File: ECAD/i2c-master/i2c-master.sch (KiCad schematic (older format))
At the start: 19 parts, among them J1 Conn_01x12_Female, J10 Conn_01x04, J11 Barrel_Jack, J12 Conn_02x10_Odd_Even, J2 Conn_01x04, J3 Conn_01x04, J4 Conn_01x04, J5 Conn_01x04, J6 Conn_01x12_Female, J7 Conn_01x04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

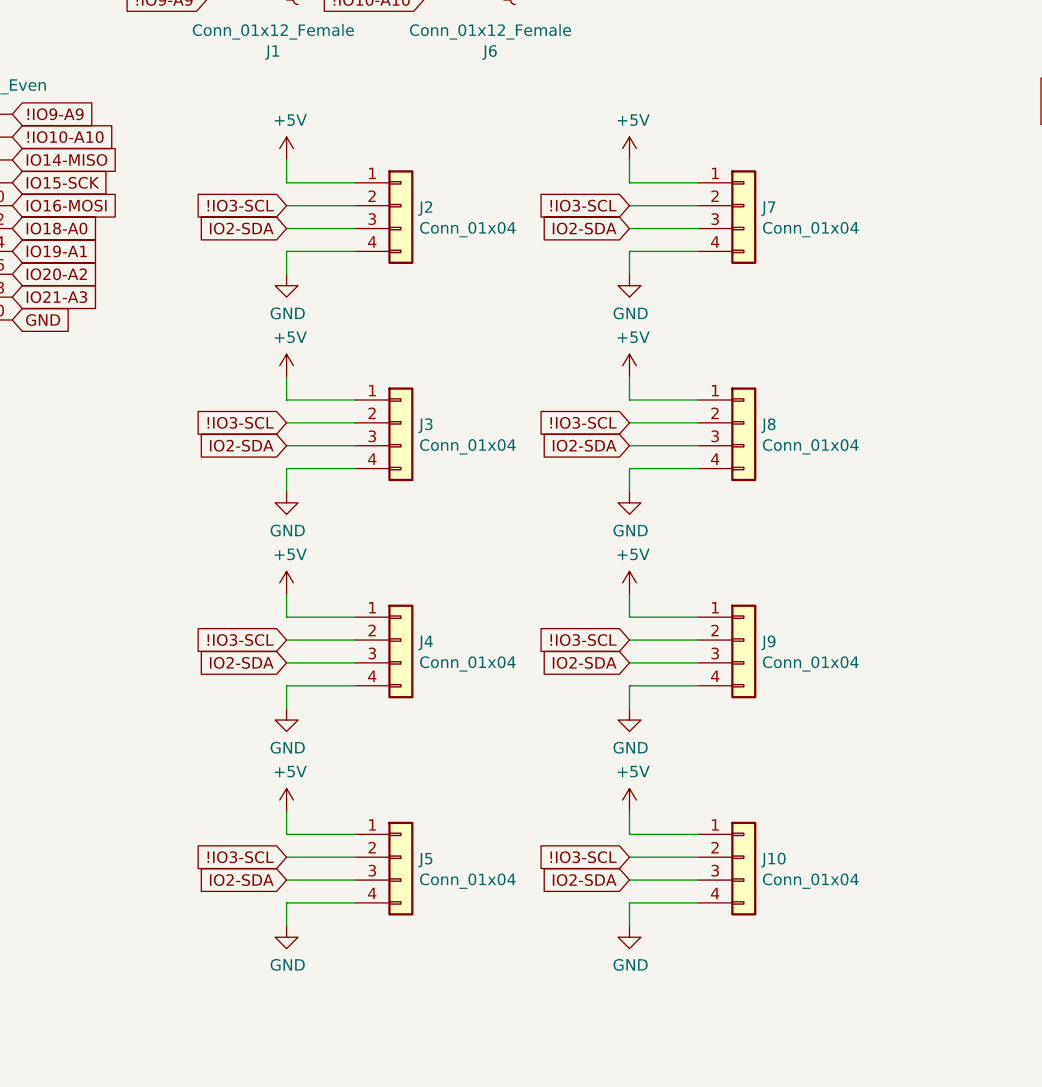
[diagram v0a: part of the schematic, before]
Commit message: Change from 1x04 2.54mm headers to 1x05 micro JST
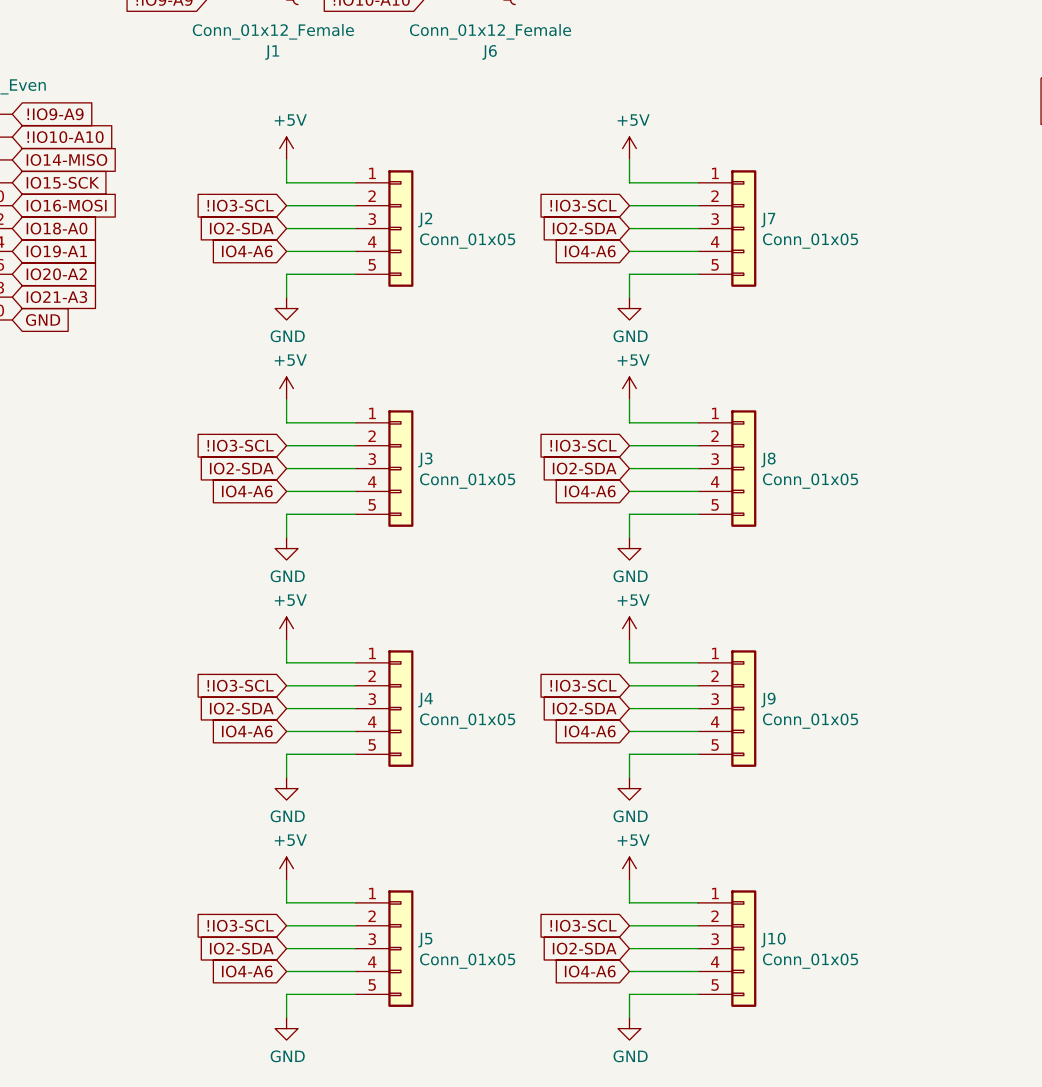
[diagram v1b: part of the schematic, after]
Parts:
- removed J10, J2, J3, J4, J5, J7, J8, J9: Conn_01x04, Connector_PinHeader_2.54mm:PinHeader_1x04_P2.54mm_Vertical, symbol Connector_Generic:Conn_01x04
- added J10, J2, J3, J4, J5, J7, J8, J9: Conn_01x05, Connector_JST:JST_GH_BM05B-GHS-TBT_1x05-1MP_P1.25mm_Vertical, symbol Connector_Generic:Conn_01x05
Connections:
- net !IO3-SCL: now also J10.2 (Pin_2), J2.2 (Pin_2), J3.2 (Pin_2), J4.2 (Pin_2), J5.2 (Pin_2), J7.2 (Pin_2), J8.2 (Pin_2), J9.2 (Pin_2)
- net +5V: now also J10.1 (Pin_1), J2.1 (Pin_1), J3.1 (Pin_1), J4.1 (Pin_1), J5.1 (Pin_1), J7.1 (Pin_1), J8.1 (Pin_1), J9.1 (Pin_1)
- net GND: now also J10.5 (Pin_5), J2.5 (Pin_5), J3.5 (Pin_5), J4.5 (Pin_5), J5.5 (Pin_5), J7.5 (Pin_5), J8.5 (Pin_5), J9.5 (Pin_5)
- net IO2-SDA: now also J10.3 (Pin_3), J2.3 (Pin_3), J3.3 (Pin_3), J4.3 (Pin_3), J5.3 (Pin_3), J7.3 (Pin_3), J8.3 (Pin_3), J9.3 (Pin_3)
- net IO4-A6: now also J10.4 (Pin_4), J2.4 (Pin_4), J3.4 (Pin_4), J4.4 (Pin_4), J5.4 (Pin_4), J7.4 (Pin_4), J8.4 (Pin_4), J9.4 (Pin_4)

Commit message: Whoops, forgot the master board
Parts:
- removed J10, J2, J3, J4, J5, J7, J8, J9: Conn_01x05, Connector_JST:JST_GH_BM05B-GHS-TBT_1x05-1MP_P1.25mm_Vertical, symbol Connector_Generic:Conn_01x05
- added J10, J2, J3, J4, J5, J7, J8, J9: Conn_01x04, Connector_JST:JST_GH_BM04B-GHS-TBT_1x04-1MP_P1.25mm_Vertical, symbol Connector_Generic:Conn_01x04
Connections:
- net !IO3-SCL: now also J10.2 (Pin_2), J2.2 (Pin_2), J3.2 (Pin_2), J4.2 (Pin_2), J5.2 (Pin_2), J7.2 (Pin_2), J8.2 (Pin_2), J9.2 (Pin_2)
- net +5V: now also J10.1 (Pin_1), J2.1 (Pin_1), J3.1 (Pin_1), J4.1 (Pin_1), J5.1 (Pin_1), J7.1 (Pin_1), J8.1 (Pin_1), J9.1 (Pin_1)
- net GND: now also J10.4 (Pin_4), J2.4 (Pin_4), J3.4 (Pin_4), J4.4 (Pin_4), J5.4 (Pin_4), J7.4 (Pin_4), J8.4 (Pin_4), J9.4 (Pin_4)
- net IO2-SDA: now also J10.3 (Pin_3), J2.3 (Pin_3), J3.3 (Pin_3), J4.3 (Pin_3), J5.3 (Pin_3), J7.3 (Pin_3), J8.3 (Pin_3), J9.3 (Pin_3)
